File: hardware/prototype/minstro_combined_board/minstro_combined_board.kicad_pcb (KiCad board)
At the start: 4 copper layers, 120 x 90 mm, 141 parts, among them J1001 VFO, J301 BATT, J401 BOOT, J402 I2C, J403 USB_C_Receptacle_USB2.0_16P, J404 SDMMC 4b, J405 Conn_Coaxial, J501 Headset, J502 SPKR, J601 FT6236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

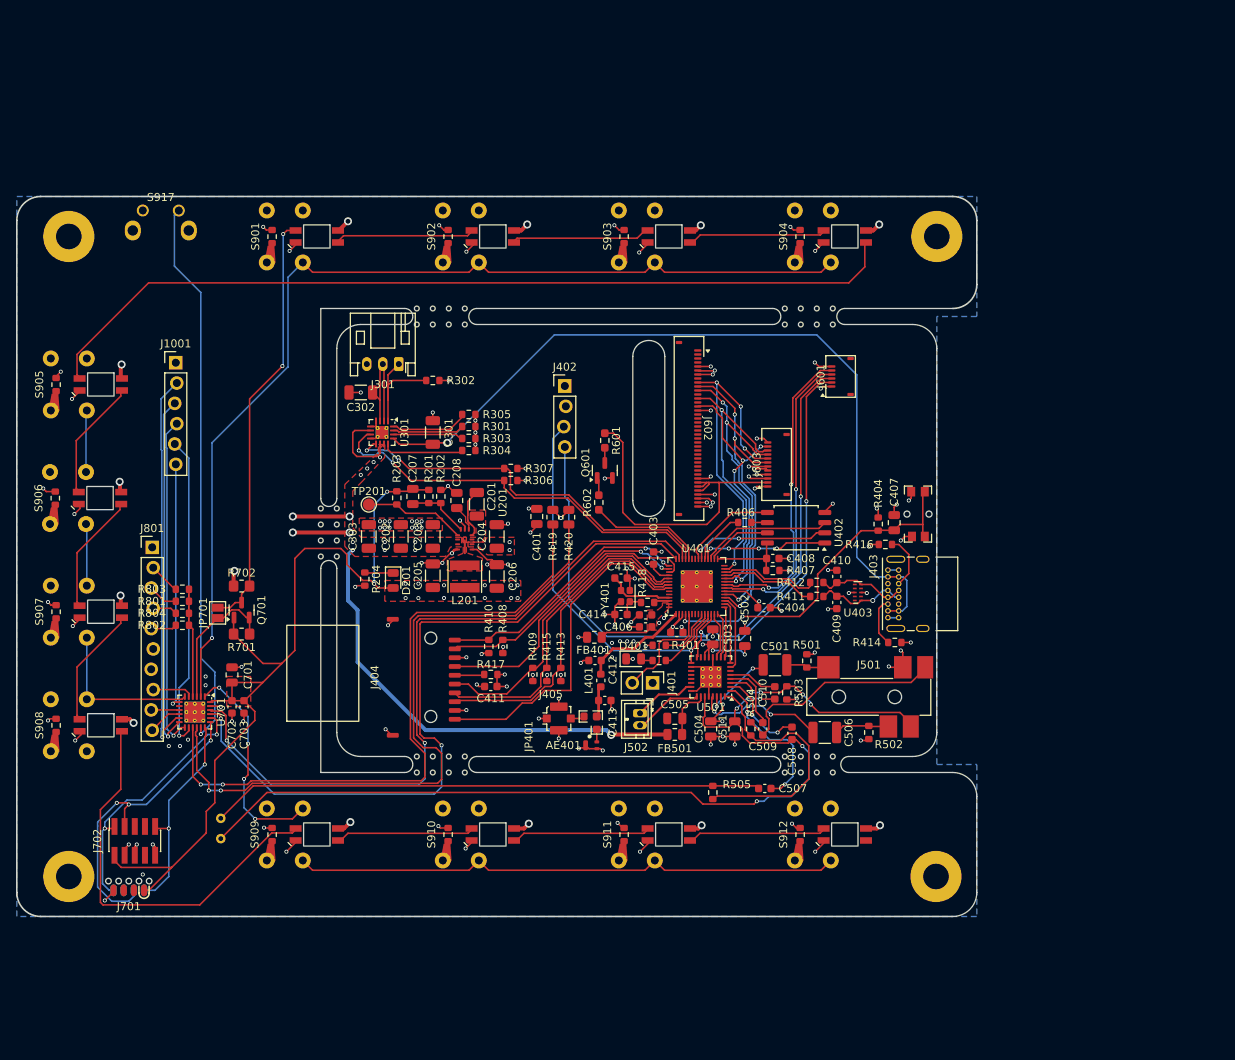
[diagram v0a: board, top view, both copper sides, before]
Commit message: Move slot and begin re-layout
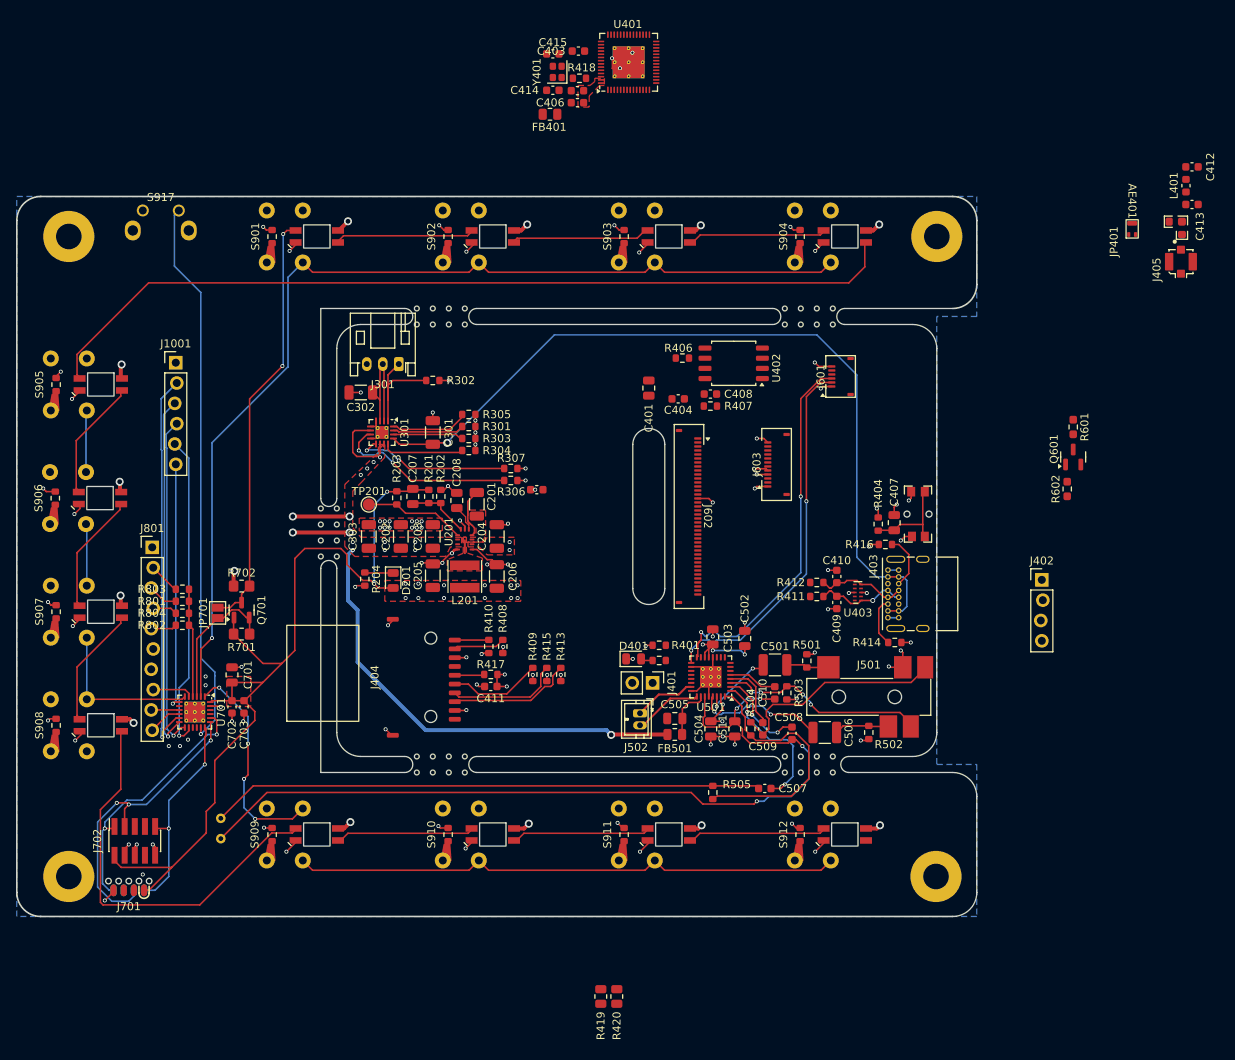
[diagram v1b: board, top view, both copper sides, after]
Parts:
- moved C412 96.8 mm to (221.9, 46.3), turned to 0 degrees
- moved J405 96.5 mm to (220.5, 58.1), turned to 180 degrees
- moved C413 96.1 mm to (221.9, 51.0)
- moved JP401 95.8 mm to (220.6, 53.1)
- moved L401 95.8 mm to (221.1, 48.6)
- moved AE401 93.5 mm to (214.4, 54.0), turned to 90 degrees
- moved C405 66.1 mm to (145.1, 36.8)
- moved C406 66.1 mm to (145.1, 38.3)
- moved C414 66.1 mm to (142.0, 36.7)
- moved C415 66.1 mm to (142.0, 32.2)
- moved R418 66.1 mm to (145.3, 35.2)
- moved U401 66.1 mm to (151.5, 33.2)
- moved Y401 66.1 mm to (142.6, 34.4)
- moved FB401 65.6 mm to (141.7, 39.7)
- moved J402 64.4 mm to (203.1, 97.9)
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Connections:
- JP401 pad 1: Net-(AE401-A) -> Net-(J405-In)
- JP401 pad 3: Net-(J405-In) -> Net-(AE401-A)
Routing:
- net /I2C_SDA: track 175.9 -> 46.2 mm, vias 5 -> 2
- net /I2C_SCL: track 175.4 -> 46.6 mm, vias 5 -> 2
- net /ESP32 Microcontroller/HMI_INT: track 94.5 -> 0.00 mm, vias 2 -> 0
- net /ESP32 Microcontroller/HMI_WAKE: track 90.9 -> 0.00 mm, vias 2 -> 0
- net /ESP32 Microcontroller/SD_DET: track 42.6 -> 0.00 mm
- net /Display Connectors/DISP_CS: track 41.5 -> 0.00 mm, vias 4 -> 0
- net /Display Connectors/DISP_DC: track 40.6 -> 0.00 mm, vias 3 -> 0
- net /Display Connectors/LED_K: track 40.5 -> 0.00 mm
- net /Display Connectors/DISP_SCL: track 39.5 -> 0.00 mm, vias 3 -> 0
- net /Display Connectors/DISP_TS_RST: track 38.0 -> 0.00 mm, vias 2 -> 0
- net /Display Connectors/DISP_TS_INT: track 37.7 -> 0.00 mm, vias 2 -> 0
- net /ESP32 Microcontroller/SD_SCK: track 37.2 -> 0.00 mm
- net /Display Connectors/DISP_SDA: track 36.6 -> 0.00 mm, vias 2 -> 0
- net +3.3V: track 178.0 -> 143.0 mm, vias 47 -> 33
- net /Display Connectors/DISP_RST: track 32.9 -> 0.00 mm, vias 4 -> 0
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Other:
- outline, holes or cut-outs redrawn

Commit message: Layout WIP
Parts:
- moved J405 96.3 mm to (142.5, 114.6)
- moved JP401 94.5 mm to (146.3, 111.5)
- moved L401 94.5 mm to (146.8, 107.0)
- moved C412 94.5 mm to (147.6, 104.6)
- moved C413 94.5 mm to (147.6, 109.3)
- moved AE401 93.2 mm to (146.7, 118.1), turned to -90 degrees
- moved C415 61.4 mm to (142.2, 93.6), turned to 90 degrees
- moved Y401 59.0 mm to (144.5, 93.4), turned to 180 degrees
- moved C403 58.9 mm to (141.5, 90.6), turned to -90 degrees
- moved FB401 58.7 mm to (148.3, 98.0), turned to 90 degrees
- moved C414 57.5 mm to (146.8, 94.0), turned to -90 degrees
- moved R418 55.4 mm to (145.3, 90.7), turned to -90 degrees
- moved C405 54.2 mm to (146.8, 90.9), turned to -90 degrees
- moved C406 52.7 mm to (148.3, 90.9), turned to -90 degrees
- moved U401 51.9 mm to (143.3, 84.5), turned to 180 degrees
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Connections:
- JP401 pad 1: Net-(J405-In) -> Net-(AE401-A)
- JP401 pad 3: Net-(AE401-A) -> Net-(J405-In)
- U401 pad 10: /ESP32 Microcontroller/STATUS_LED -> unconnected-(U401-GPIO5-Pad10)
- U401 pad 51: unconnected-(U401-GPIO45-Pad51) -> /ESP32 Microcontroller/STATUS_LED
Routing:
- net /I2C_SDA: track 46.2 -> 166.4 mm, vias 2 -> 8
- net /I2C_SCL: track 46.6 -> 162.5 mm, vias 2 -> 6
- net /ESP32 Microcontroller/USB_uC_N: track 0.00 -> 82.0 mm, vias 0 -> 2
- net /ESP32 Microcontroller/USB_uC_P: track 0.00 -> 80.5 mm, vias 0 -> 2
- net /ESP32 Microcontroller/HMI_INT: track 0.00 -> 80.2 mm, vias 0 -> 2
- net /Display Connectors/DISP_BL: track 0.00 -> 79.6 mm
- net /ESP32 Microcontroller/HMI_WAKE: track 0.00 -> 77.7 mm, vias 0 -> 2
- net /ESP32 Microcontroller/CHIP_EN: track 10.9 -> 67.1 mm
- net /Audio/I2S_FS: track 0.00 -> 46.4 mm, vias 0 -> 2
- net /Audio/I2S_BCLK: track 0.00 -> 44.4 mm, vias 0 -> 2
- net /Audio/I2S_ADCOUT: track 0.00 -> 42.2 mm, vias 0 -> 2
- net /Display Connectors/DISP_TS_RST: track 0.00 -> 41.9 mm, vias 0 -> 2
- net /Audio/I2S_ADCIN: track 0.00 -> 41.0 mm, vias 0 -> 2
- net /Display Connectors/DISP_RST: track 0.00 -> 40.8 mm, vias 0 -> 3
- net /Display Connectors/DISP_TS_INT: track 0.00 -> 40.5 mm, vias 0 -> 2
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
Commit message: Adjust connector positions, thicken Vusb traces, move onboard microphone, improve silkscreen
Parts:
- added G***: LOGO, BVH_Logos:SkyIron_logo_Back, F.Cu at (105.8, 75.5)
- added G***: LOGO, BVH_Logos:SkyIron_logo_Back, F.Cu at (128.9, 75.2)
- moved SW401 18.1 mm to (188.2, 71.6)
- moved J402 14.4 mm to (170.7, 76.0), turned to 90 degrees
- moved J601 11.3 mm to (184.2, 82.0)
- moved J603 8.28 mm to (177.5, 87.0)
- moved MK501 2.40 mm to (96.6, 129.0)
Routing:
- net /ESP32 Microcontroller/CHIP_EN: track 67.1 -> 84.1 mm
- net /Display Connectors/DISP_BL: track 79.6 -> 94.6 mm
- net /Display Connectors/DISP_TS_RST: track 41.9 -> 54.3 mm
- net /Display Connectors/DISP_TS_INT: track 40.5 -> 52.9 mm
- net /Display Connectors/LED_K: track 22.1 -> 30.2 mm
- net /Display Connectors/DISP_CS: track 39.6 -> 47.4 mm
- net /Display Connectors/DISP_SDA: track 39.8 -> 47.6 mm
- net /Display Connectors/DISP_SCL: track 36.1 -> 43.9 mm
- net /Display Connectors/DISP_RST: track 40.8 -> 48.1 mm
- net /Display Connectors/DISP_DC: track 35.9 -> 41.3 mm
- net +3.3V: track 169.4 -> 174.9 mm, vias 45 -> 46
- net GND: track 154.8 -> 150.9 mm, vias 117 -> 114
- net /Battery/Vusb: track 102.2 -> 104.9 mm
- net /I2C_SCL: track 162.5 -> 159.9 mm, vias 6 -> 5
- net /Audio/Mic_P: track 69.0 -> 71.4 mm
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- added copper zone on F.Cu, net /Battery/Vusb
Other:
- board text added: "3.3V"
- board text added: "A"
- board text added: "A OD"
- board text added: "AB4EN Minstro HMI v1 2025-JUN-12"
- board text added: "AB4EN Minstro MPU v1 2025-JUN-12"
- board text added: "B"
- board text added: "B OD"
- board text added: "FT6236 Touch"
- board text added: "GND"
- board text added: "ILI9488 Display"
- board text added: "NAV"
- board text added: "Pop only if no temp sensor"
- board text added: "RESET"
- board text added: "SCL"
- board text added: "SDA"
- board text added: "ST7789 Display"
- board text added: "SW"
- board text added: "VFO"
